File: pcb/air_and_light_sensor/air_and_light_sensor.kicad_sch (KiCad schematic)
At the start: 0 parts

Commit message: generating the GERBERS
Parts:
- added J10: Screw_Terminal_01x04, TerminalBlock_Phoenix:TerminalBlock_Phoenix_MKDS-1,5-4_1x04_P5.00mm_Horizontal, symbol Connector:Screw_Terminal_01x04
- added R4: VT93xx, OptoDevice:R_LDR_4.9x4.2mm_P2.54mm_Vertical, symbol Sensor_Optical:VT93xx
- added R5: 10k, Resistor_SMD:R_0603_1608Metric_Pad0.98x0.95mm_HandSolder, symbol Device:R
- added U3: AM2302, Sensor:ASAIR_AM2302_P2.54mm_Lead2.75mm_TabDown, symbol Sensor:AM2302
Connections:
- new net: J10.2 (Pin_2), U3.2 (SDA)
- new net: J10.3 (Pin_3), R4.2, R5.1
- new net GND: J10.1 (Pin_1), R5.2, U3.3 (GND), U3.4 (GND)
- new net VDD: J10.4 (Pin_4), R4.1, U3.1 (VDD)

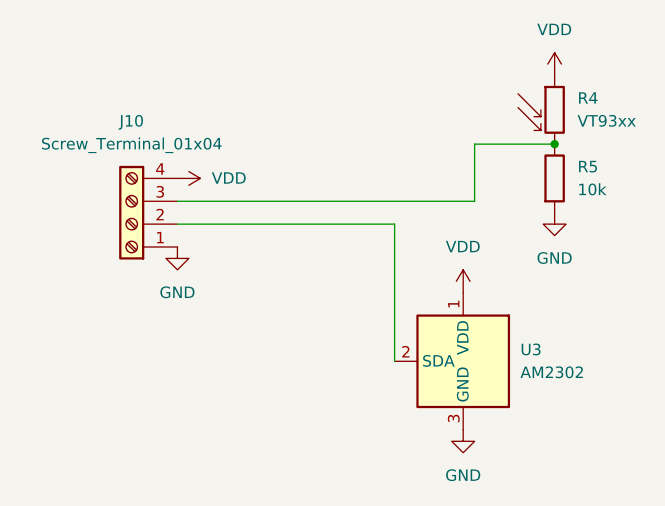
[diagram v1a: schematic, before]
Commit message: adding pulldown resistor to the SensorBoard
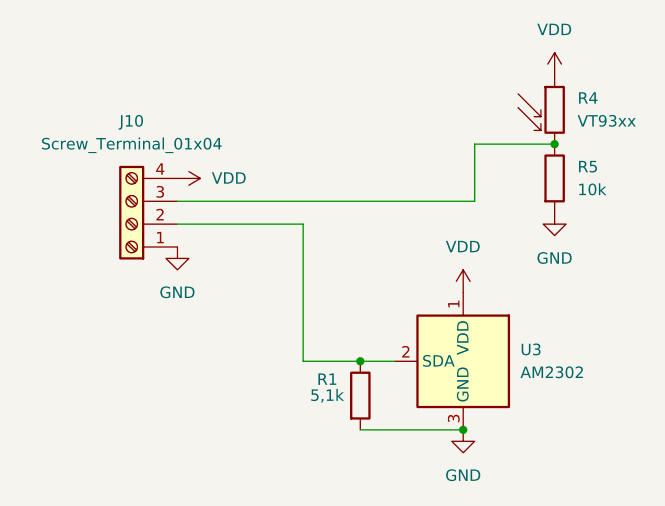
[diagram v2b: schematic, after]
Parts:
- added R1: 5,1k, Resistor_SMD:R_0603_1608Metric_Pad0.98x0.95mm_HandSolder, symbol Device:R
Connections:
- net GND: now also R1.2
- net at J10.2 (Pin_2), U3.2 (SDA): now also R1.1
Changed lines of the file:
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@@
 	(paper "A4")
+	(junction
+		(at 154.94 130.81)
+		(diameter 0)
+		(color 0 0 0 0)
+	)
 	(junction
 		(at 165.1 99.06)
@@
 		(color 0 0 0 0)
 	)
+	(junction
+		(at 143.51 123.19)
+		(diameter 0)
+		(color 0 0 0 0)
+	)
 	(wire
 		(pts
@@
 	(wire
 		(pts
-			(xy 123.19 107.95) (xy 147.32 107.95)
+			(xy 123.19 107.95) (xy 137.16 107.95)
 		)
 		(stroke
@@
 	(wire
 		(pts
-			(xy 123.19 105.41) (xy 156.21 105.41)
+			(xy 143.51 123.19) (xy 147.32 123.19)
 		)
 		(stroke
@@
 	(wire
 		(pts
-			(xy 156.21 99.06) (xy 165.1 99.06)
+			(xy 123.19 105.41) (xy 156.21 105.41)
 		)
 		(stroke
@@
 	(wire
 		(pts
-			(xy 147.32 107.95) (xy 147.32 123.19)
+			(xy 137.16 123.19) (xy 143.51 123.19)
+		)
+		(stroke
+			(width 0)
+			(type default)
+		)
+	)
+	(wire
+		(pts
+			(xy 143.51 130.81) (xy 154.94 130.81)
+		)
+		(stroke
+			(width 0)
+			(type default)
+		)
+	)
+	(wire
+		(pts
+			(xy 156.21 99.06) (xy 165.1 99.06)
+		)
+		(stroke
+			(width 0)
+			(type default)
+		)
+	)
+	(wire
+		(pts
+			(xy 137.16 107.95) (xy 137.16 123.19)
 		)
 		(stroke
@@
 	)
 	(symbol
+		(lib_id "Device:R")
+		(at 143.51 127 0)
+		(unit 1)
+		(body_style 1)
+		(exclude_from_sim no)
+		(in_bom yes)
+		(on_board yes)
+		(in_pos_files yes)
+		(dnp no)
+		(property "Reference" "R1"
+			(at 138.684 125.222 0)
+			(show_name no)
+			(do_not_autoplace no)
+			(effects
+				(font
+					(size 1.27 1.27)
+				)
+				(justify left)
+			)
+		)
+		(property "Value" "5,1k"
+			(at 137.922 127 0)
+			(show_name no)
+			(do_not_autoplace no)
+			(effects
+				(font
+					(size 1.27 1.27)
+				)
+				(justify left)
+			)
+		)
+		(property "Footprint" "Resistor_SMD:R_0603_1608Metric_Pad0.98x0.95mm_HandSolder"
+			(at 141.732 127 90)
+			(hide yes)
+			(show_name no)
+			(do_not_autoplace no)
+			(effects
+				(font
+					(size 1.27 1.27)
+				)
+			)
+		)
+		(property "Datasheet" ""
+			(at 143.51 127 0)
+			(hide yes)
+			(show_name no)
+			(do_not_autoplace no)
+			(effects
+				(font
+					(size 1.27 1.27)
+				)
+			)
+		)
+		(property "Description" "Resistor"
+			(at 143.51 127 0)
+			(hide yes)
+			(show_name no)
+			(do_not_autoplace no)
+			(effects
+				(font
+					(size 1.27 1.27)
+				)
+			)
+		)
+		(pin "2"
+		)
+		(pin "1"
+		)
+		(instances
+			(project "air_and_light_sensor"
+				(path "/e38711c9-d65a-4585-9eaf-05baf53ac0c4"
+					(reference "R1")
+					(unit 1)
+				)
+			)
+		)
+	)
+	(symbol
 		(lib_id "Connector:Screw_Terminal_01x04")
 		(at 118.11 107.95 180)
@@
 		(lib_id "power:GND")
 		(at 154.94 130.81 0)
+		(mirror y)
 		(unit 1)
 		(body_style 1)
@@
 		(in_pos_files yes)
 		(dnp no)
-		(fields_autoplaced yes)
 		(property "Reference" "#PWR02"
 			(at 154.94 137.16 0)

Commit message: merging the BOMs
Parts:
- R1: jlc part # (none) -> C177348
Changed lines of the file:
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@@
+			)
+		)
+		(property "jlc part #" "C177348"
+			(at 143.51 127 0)
+			(hide yes)
+			(show_name no)
+			(do_not_autoplace no)
+			(effects
+				(font
+					(size 1.27 1.27)
+				)
 			)
 		)
